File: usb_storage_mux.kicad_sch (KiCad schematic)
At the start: 26 parts, among them J7 USB3_B, J8 Hirose USB3_B_Micro, J9 USB3_A, U6 TMUXHS4212

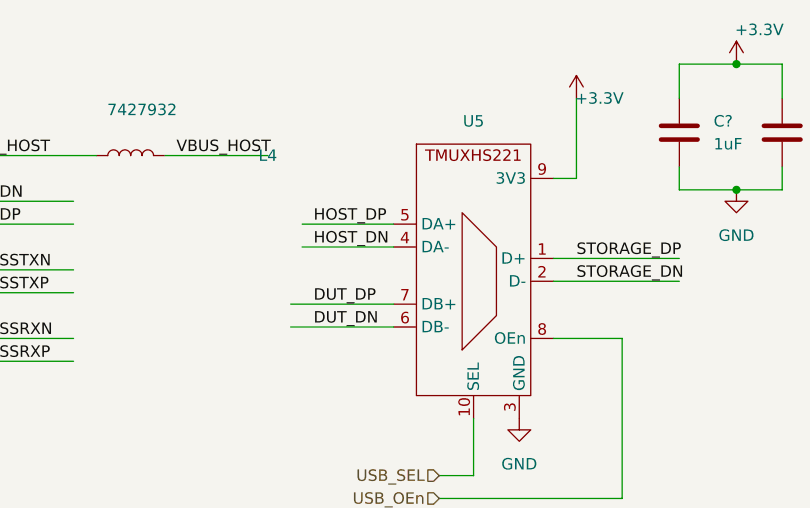
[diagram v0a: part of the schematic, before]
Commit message: Reorganized repo with rename to dutlink 1.1.0
Signed-off-by: Miguel Angel Ajo Pelayo <majopela@redhat.com>
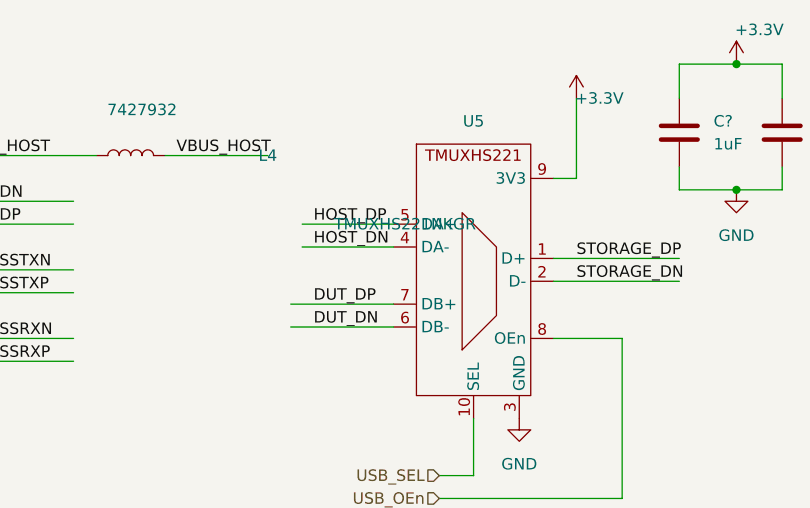
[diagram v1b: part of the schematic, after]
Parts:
- C? (x2): MFN (none) -> HV470M035E055ETR
- C? (x2): footprint Capacitor_SMD:C_0402_1005Metric -> Capacitor_SMD:C_0603_1608Metric; MFN (none) -> CL10B105KA8NNNC
- C? (x2): footprint Capacitor_SMD:C_0402_1005Metric -> Capacitor_SMD:C_0603_1608Metric; MFN (none) -> CL10B104KB8NNNC
- C? (x3): footprint Capacitor_SMD:C_0402_1005Metric -> Capacitor_SMD:C_0603_1608Metric
- J7: Link (none) -> https://es.farnell.com/wurth-elektronik/692221030100/usb-3-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; MFN (none) -> 692221030100
- J9: Link (none) -> https://es.farnell.com/molex/48393-0003/conector-usb-3-0-us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; MFN (none) -> 48393-0003
- Q? (x2): MFN (none) -> FDC6330L
- R? (x2): MFN (none) -> RC0603JR-0747KL
- R? (x2): MFN (none) -> RC0603FR-072K2L
- R? (x2): MFN (none) -> RC0603FR-070RL
- U5: value ~ -> TMUXHS221NKGR; Link (none) -> https://eu.mouser.com/ProductDetail/Texas-Instruments/TMUXH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; MFN (none) -> TMUXHS221NKGR
- U6: MFN (none) -> TMUXHS4212RKSR
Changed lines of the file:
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@@
+      (effects (font (size 1.27 1.27)) hide)
+    )
+    (property "MFN" "RC0603JR-0747KL" (at 195.58 85.09 0)
       (effects (font (size 1.27 1.27)) hide)
     )
@@
       (effects (font (size 1.27 1.27)) hide)
     )
+    (property "MFN" "HV470M035E055ETR" (at 222.25 39.37 0)
+      (effects (font (size 1.27 1.27)) hide)
+    )
     (pin "1")
     (pin "2")
@@
     )
     (property "Datasheet" "https://www.onsemi.com/pub/Collateral/FDC6330L-D.PDF" (at 207.01 90.17 0)
+      (effects (font (size 1.27 1.27)) hide)
+    )
+    (property "MFN" "FDC6330L" (at 209.55 87.63 0)
       (effects (font (size 1.27 1.27)) hide)
     )
@@
       (effects (font (size 1.27 1.27)) (justify left))
     )
-    (property "Footprint" "Capacitor_SMD:C_0402_1005Metric" (at 158.4452 146.05 0)
+    (property "Footprint" "Capacitor_SMD:C_0603_1608Metric" (at 158.4452 146.05 0)
       (effects (font (size 1.27 1.27)) hide)
     )
     (property "Datasheet" "~" (at 157.48 142.24 0)
+      (effects (font (size 1.27 1.27)) hide)
+    )
+    (property "MFN" "CL10B105KA8NNNC" (at 157.48 142.24 0)
       (effects (font (size 1.27 1.27)) hide)
     )
@@
       (effects (font (size 1.27 1.27)) hide)
     )
+    (property "MFN" "RC0603JR-0747KL" (at 194.31 40.64 0)
+      (effects (font (size 1.27 1.27)) hide)
+    )
     (pin "1")
     (pin "2")
@@
       (effects (font (size 1.27 1.27)) hide)
     )
+    (property "MFN" "RC0603FR-072K2L" (at 208.28 57.15 0)
+      (effects (font (size 1.27 1.27)) hide)
+    )
     (pin "1")
     (pin "2")
@@
     )
     (property "Datasheet" "~" (at 35.56 46.99 0)
+      (effects (font (size 1.27 1.27)) hide)
+    )
+    (property "Link" "https://es.farnell.com/wurth-elektronik/692221030100/usb-3-0-tipo-b-hembra-th/dp/1861259?gclid=EAIaIQobChMIj5-17u_P_wIV9RsGAB1SZQeBEAAYASAAEgJnLPD_BwE&mckv=s_dc|pcrid|509002904386|kword|692221030100|match|p|plid||slid||product||pgrid|119454722043|ptaid|aud-1702385753400:kwd-25618251422|&CMP=KNC-GES-GEN-SKU-MDC-Connectors-Cable-Test-OOSandAudienceOpt-14-Feb-23" (at 31.75 49.53 0)
+      (effects (font (size 1.27 1.27)) hide)
+    )
+    (property "MFN" "692221030100" (at 31.75 49.53 0)
       (effects (font (size 1.27 1.27)) hide)
     )
@@
       (effects (font (size 1.27 1.27)) (justify left))
     )
-    (property "Footprint" "Capacitor_SMD:C_0402_1005Metric" (at 169.8752 146.05 0)
+    (property "Footprint" "Capacitor_SMD:C_0603_1608Metric" (at 169.8752 146.05 0)
       (effects (font (size 1.27 1.27)) hide)
     )
@@
       (effects (font (size 1.27 1.27)) hide)
     )
+    (property "MFN" "CL10B104KB8NNNC" (at 168.91 142.24 0)
+      (effects (font (size 1.27 1.27)) hide)
+    )
     (pin "1")
     (pin "2")
@@
       (effects (font (size 1.27 1.27)) (justify left))
     )
-    (property "Footprint" "Capacitor_SMD:C_0402_1005Metric" (at 33.9852 190.5 0)
+    (property "Footprint" "Capacitor_SMD:C_0603_1608Metric" (at 33.9852 190.5 0)
       (effects (font (size 1.27 1.27)) hide)
     )
@@
     )
     (property "Datasheet" "~" (at 256.54 105.41 0)
+      (effects (font (size 1.27 1.27)) hide)
+    )
+    (property "Link" "https://es.farnell.com/molex/48393-0003/conector-usb-3-0-usb-tipo-a-hembra/dp/2401595?gclid=EAIaIQobChMIxd3h57zR_wIVppRoCR0T3AuaEAAYASAAEgJqavD_BwE&mckv=s_dc|pcrid|508918265685|kword|48393%200003|match|p|plid||slid||product||pgrid|121108853698|ptaid|aud-1702385753400:kwd-64953266167|&CMP=KNC-GES-GEN-SKU-MDC-Connectors-Cable-Test-OOSandAudienceOpt-14-Feb-23" (at 260.35 107.95 0)
+      (effects (font (size 1.27 1.27)) hide)
+    )
+    (property "MFN" "48393-0003" (at 260.35 107.95 0)
       (effects (font (size 1.27 1.27)) hide)
     )
@@
       (effects (font (size 1.27 1.27)) hide)
     )
+    (property "MFN" "FDC6330L" (at 208.28 43.18 0)
+      (effects (font (size 1.27 1.27)) hide)
+    )
     (pin "1")
     (pin "2")
@@
       (effects (font (size 1.27 1.27)) hide)
     )
+    (property "MFN" "RC0603FR-070RL" (at 123.19 97.79 0)
+      (effects (font (size 1.27 1.27)) hide)
+    )
     (pin "1")
     (pin "2")
@@
       (effects (font (size 1.27 1.27)) (justify left))
     )
-    (property "Footprint" "Capacitor_SMD:C_0402_1005Metric" (at 127.9652 40.64 0)
+    (property "Footprint" "Capacitor_SMD:C_0603_1608Metric" (at 127.9652 40.64 0)
       (effects (font (size 1.27 1.27)) hide)
     )
@@
       (effects (font (size 1.27 1.27)) hide)
     )
+    (property "MFN" "CL10B105KA8NNNC" (at 127 36.83 0)
+      (effects (font (size 1.27 1.27)) hide)
+    )
     (pin "1")
     (pin "2")
@@
     )
     (property "Datasheet" "https://www.ti.com/lit/ds/symlink/tmuxhs4212.pdf" (at 119.38 102.87 0)
+      (effects (font (size 1.27 1.27)) hide)
+    )
+    (property "MFN" "TMUXHS4212RKSR" (at 119.38 102.87 0)
       (effects (font (size 1.27 1.27)) hide)
     )
@@
       (effects (font (size 1.27 1.27)) (justify left))
     )
-    (property "Footprint" "Capacitor_SMD:C_0402_1005Metric" (at 31.4452 83.82 0)
+    (property "Footprint" "Capacitor_SMD:C_0603_1608Metric" (at 31.4452 83.82 0)
       (effects (font (size 1.27 1.27)) hide)
     )
@@
       (effects (font (size 1.27 1.27)) (justify left))
     )
-    (property "Footprint" "Capacitor_SMD:C_0402_1005Metric" (at 139.3952 40.64 0)
+    (property "Footprint" "Capacitor_SMD:C_0603_1608Metric" (at 139.3952 40.64 0)
       (effects (font (size 1.27 1.27)) hide)
     )
@@
       (effects (font (size 1.27 1.27)) hide)
     )
+    (property "MFN" "CL10B104KB8NNNC" (at 138.43 36.83 0)
+      (effects (font (size 1.27 1.27)) hide)
+    )
     (pin "1")
     (pin "2")
@@
       (effects (font (size 1.27 1.27)) hide)
     )
+    (property "MFN" "HV470M035E055ETR" (at 226.06 83.82 0)
+      (effects (font (size 1.27 1.27)) hide)
+    )
     (pin "1")
     (pin "2")
@@
       (effects (font (size 1.27 1.27)))
     )
-    (property "Value" "~" (at 96.52 46.99 0)
+    (property "Value" "TMUXHS221NKGR" (at 96.52 46.99 0)
       (effects (font (size 1.27 1.27)))
     )
@@
     )
     (property "Datasheet" "https://www.ti.com/product/TMUXHS221" (at 96.52 46.99 0)
+      (effects (font (size 1.27 1.27)) hide)
+    )
+    (property "Link" "https://eu.mouser.com/ProductDetail/Texas-Instruments/TMUXHS221NKGR?qs=IPgv5n7u5QbuI%2Forjo3H9g%3D%3D" (at 96.52 46.99 0)
+      (effects (font (size 1.27 1.27)) hide)
+    )
+    (property "MFN" "TMUXHS221NKGR" (at 96.52 46.99 0)
       (effects (font (size 1.27 1.27)) hide)
     )
@@
       (effects (font (size 1.27 1.27)) hide)
     )
+    (property "MFN" "RC0603FR-072K2L" (at 209.55 101.6 0)
+      (effects (font (size 1.27 1.27)) hide)
+    )
     (pin "1")
     (pin "2")
@@
       (effects (font (size 1.27 1.27)) (justify left))
     )
-    (property "Footprint" "Capacitor_SMD:C_0402_1005Metric" (at 272.7452 142.24 0)
+    (property "Footprint" "Capacitor_SMD:C_0603_1608Metric" (at 272.7452 142.24 0)
       (effects (font (size 1.27 1.27)) hide)
     )
@@
       (effects (font (size 1.27 1.27)) hide)
     )
+    (property "MFN" "RC0603FR-070RL" (at 128.27 97.79 0)
+      (effects (font (size 1.27 1.27)) hide)
+    )

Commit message: 2.0.0 release
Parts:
- removed C?: 47uF 32V, Capacitor_SMD:CP_Elec_6.3x5.4_Nichicon, symbol Device:C_Polarized
- removed C? (x3): 100nF, Capacitor_SMD:C_0603_1608Metric, symbol Device:C
- removed J7: USB3_B, USB3Wurth:Wurth WR-COM USB 3.0 692221030100, symbol Connector:USB3_B
- removed L4: 7427932, FOOTPRINTS:7427932, symbol Device:L
- removed R? (x3): 330, Resistor_SMD:R_0402_1005Metric, symbol Device:R
- removed R? (x2): 0, Resistor_SMD:R_0603_1608Metric, symbol Device:R
- added C25, C26, C27, C28: 100nF, Capacitor_SMD:C_0402_1005Metric, symbol Device:C_Small
- added C? (x2): 100nF, Capacitor_SMD:C_0402_1005Metric, symbol Device:C
- added D8: 1N4448WT, Diode_SMD:D_SOD-523, symbol Diode:1N4448WT
- added F2: MF-MSMF125-2, FOOTPRINTS:MF-MSMF125-2, symbol Device:Polyfuse
- added R? (x2): 330, Resistor_SMD:R_0402_1005Metric, symbol Device:R
- C? (x2): MPN (none) -> CL10B105KA8NNNC
- C? (x2): footprint Capacitor_SMD:C_0603_1608Metric -> Capacitor_SMD:C_0402_1005Metric; MPN (none) -> CL05B104K05NNNC; MPN2 (none) -> TCC0402X7R104M160AT
- C?: MPN (none) -> HV470M035E055ETR
- J9: Link https://es.farnell.com/molex/48393-0003/conector-usb-3-0-us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 -> https://eu.mouser.com/ProductDetail/Molex/48393-0001?qs=4Ef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; MFN 48393-0003 -> 48393-0001; MPN (none) -> 48393-0001
- Q? (x2): Link (none) -> https://www.mouser.es/ProductDetail/onsemi-Fairchild/FDC633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; MPN (none) -> FDC6330L
- R? (x2): footprint Resistor_SMD:R_0603_1608Metric -> Resistor_SMD:R_0402_1005Metric; MFN RC0603JR-0747KL -> RTT024702FTH; MPN (none) -> RTT024702FTH
- R? (x2): footprint Resistor_SMD:R_0603_1608Metric -> Resistor_SMD:R_0402_1005Metric; MFN RC0603FR-072K2L -> RTT022201FTH; MPN (none) -> RTT022201FTH
- U5: value TMUXHS221NKGR -> TMUXHS221; MPN (none) -> TMUXHS221NKGR
- U6: Link (none) -> https://eu.mouser.com/ProductDetail/Texas-Instruments/TMUXH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; MPN (none) -> TMUXHS4212RKSR
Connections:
- net +3.3V: now also U6.1 (RSVD1), U6.10 (RSVD2)
- net DUT_SSRXN: now also C25.1; no longer U6.14 (C0n)
- net DUT_SSRXP: now also C26.1; no longer U6.15 (C0p)
- net GND: now also C?.2, C?.2, R?.1, R?.1
- net STORAGE_SSRXN: now also U6.4 (A0n); no longer U6.8 (A1n)
- net STORAGE_SSRXP: now also U6.3 (A0p); no longer U6.7 (A1p)
- net STORAGE_SSTXN: now also C27.2; no longer U6.4 (A0n)
- net STORAGE_SSTXP: now also C28.2; no longer U6.3 (A0p)
- net VBUS_STORAGE: now also F2.1; no longer J9.1 (VBUS)
- net at J8.11 (SHIELD): now also C?.1, R?.2
- net at J9.10 (SHIELD): now also C?.1, R?.2
- net HOST_DN renamed SHOST_DN
- net HOST_DP renamed SHOST_DP
- net HOST_SSRXN renamed SHOST_SSRXN
- net HOST_SSRXP renamed SHOST_SSRXP
- net HOST_SSTXN renamed SHOST_SSTXN
- net HOST_SSTXP renamed SHOST_SSTXP
- net VBUS_HOST renamed +5V
- new net HUB_PRTCTL: D8.2 (A)
- new net VBUS_STORAGE_: D8.1 (K), F2.2, J9.1 (VBUS)
- new net _DUT_SSRXN: C25.2, U6.14 (C0n)
- new net _DUT_SSRXP: C26.2, U6.15 (C0p)
- new net _STORAGE_SSTXN: C27.1, U6.8 (A1n)
- new net _STORAGE_SSTXP: C28.1, U6.7 (A1p)
- no-connect marks 0 -> 1
